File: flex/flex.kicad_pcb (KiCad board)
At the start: 2 copper layers, 104.8 x 90.6 mm, 73 parts, among them J1 Conn_01x04_Female, J2 Conn_01x05_Female, J3 Conn_01x03_Female, J4 Conn_01x06_Female, J5 Conn_01x03_Female, SW10 SW_Push, SW11 SW_Push, SW12 SW_Push, SW15 SW_Push, SW16 SW_Push, SW17 SW_Push, SW20 SW_Push, SW21 SW_Push, SW22 SW_Push, SW24 SW_Push, SW25 SW_Push, SW26 SW_Push, SW6 SW_Push, SW7 SW_Push, SW8 SW_Push

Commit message: licenses
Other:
- board text added: "Licensed under CC BY-NC-SA 4.0 Copyright Quentin Lebastard 2022"

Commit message: edge cuts
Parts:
- added C1: C, libs:D_0402, F.Cu at (43.2, 75.8)
- added D25: 1N4148, libs:D_SOD-523, F.Cu at (75.8, 122.1)
- added D26: 1N4148, libs:D_SOD-523, F.Cu at (75.8, 123.3)
- added D8: 1N4148, libs:D_SOD-523, F.Cu at (75.8, 124.6)
- added R1: R, libs:D_0402, F.Cu at (43.2, 74.5)
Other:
- board size 104.8 x 90.6 mm -> 104.1 x 90.6 mm

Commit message: PCB settigs
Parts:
- removed the C1 at (43.2, 75.8)
- removed the D25 at (75.8, 122.1)
- removed the D26 at (75.8, 123.3)
- removed the D8 at (75.8, 124.6)
- removed the R1 at (43.2, 74.5)
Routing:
- net Gnd: track 613.5 -> 0.00 mm, vias 22 -> 0
- net Vcc: track 601.7 -> 0.00 mm, vias 16 -> 0
- net row2: track 460.2 -> 0.00 mm, vias 5 -> 0
- net row4: track 347.7 -> 0.00 mm, vias 8 -> 0
- net row3: track 294.0 -> 0.00 mm, vias 3 -> 0
- net col2: track 288.4 -> 0.00 mm, vias 8 -> 0
- net col6: track 174.7 -> 0.00 mm, vias 7 -> 0
- net col5: track 158.5 -> 0.00 mm, vias 6 -> 0
- net col3: track 157.7 -> 0.00 mm, vias 7 -> 0
- net Net-(D41-Pad1): track 147.8 -> 0.00 mm, vias 3 -> 0
- net Net-(D25-Pad1): track 129.5 -> 0.00 mm, vias 2 -> 0
- net col4: track 128.3 -> 0.00 mm, vias 5 -> 0
- net Net-(D21-Pad3): track 122.1 -> 0.00 mm, vias 3 -> 0
- net Net-(D51-Pad1): track 103.0 -> 0.00 mm, vias 3 -> 0
- net Net-(D5-Pad3): track 54.8 -> 0.00 mm, vias 3 -> 0
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
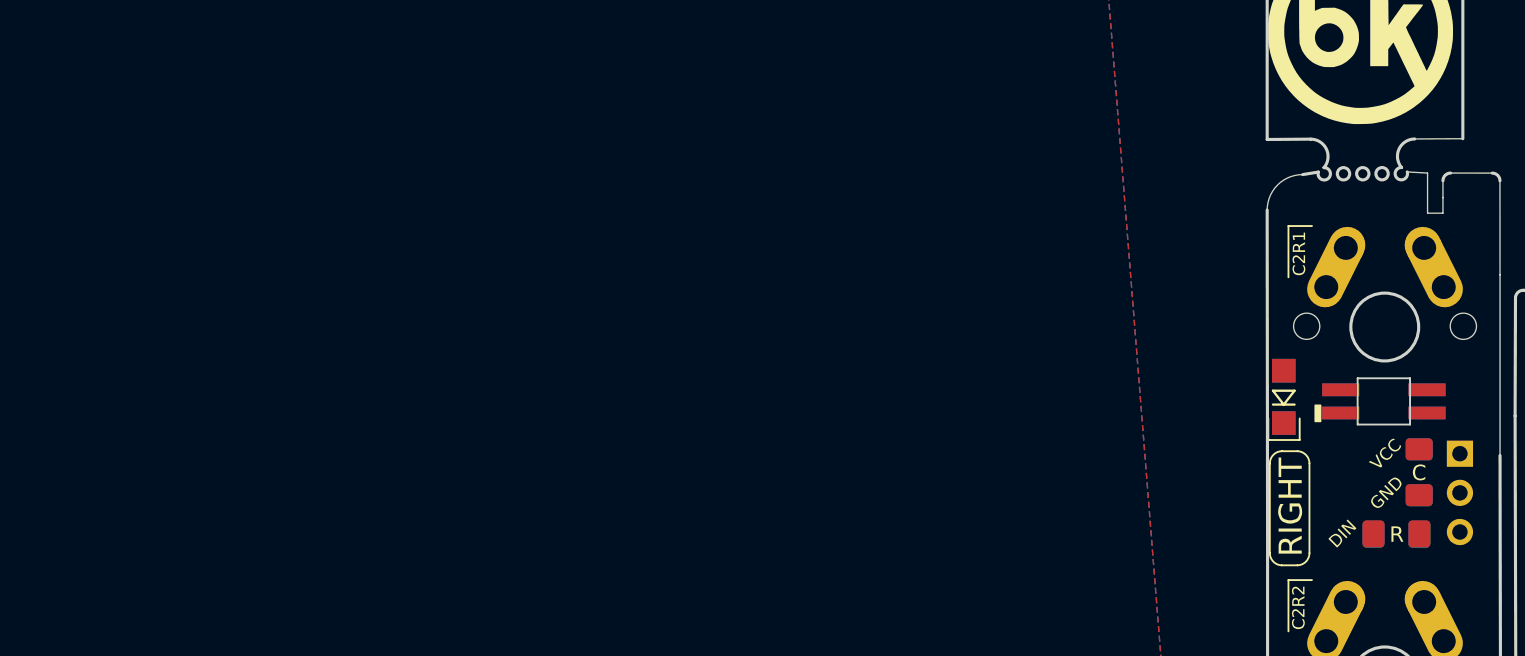
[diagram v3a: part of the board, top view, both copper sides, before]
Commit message: cleanup schem, reversible r and c
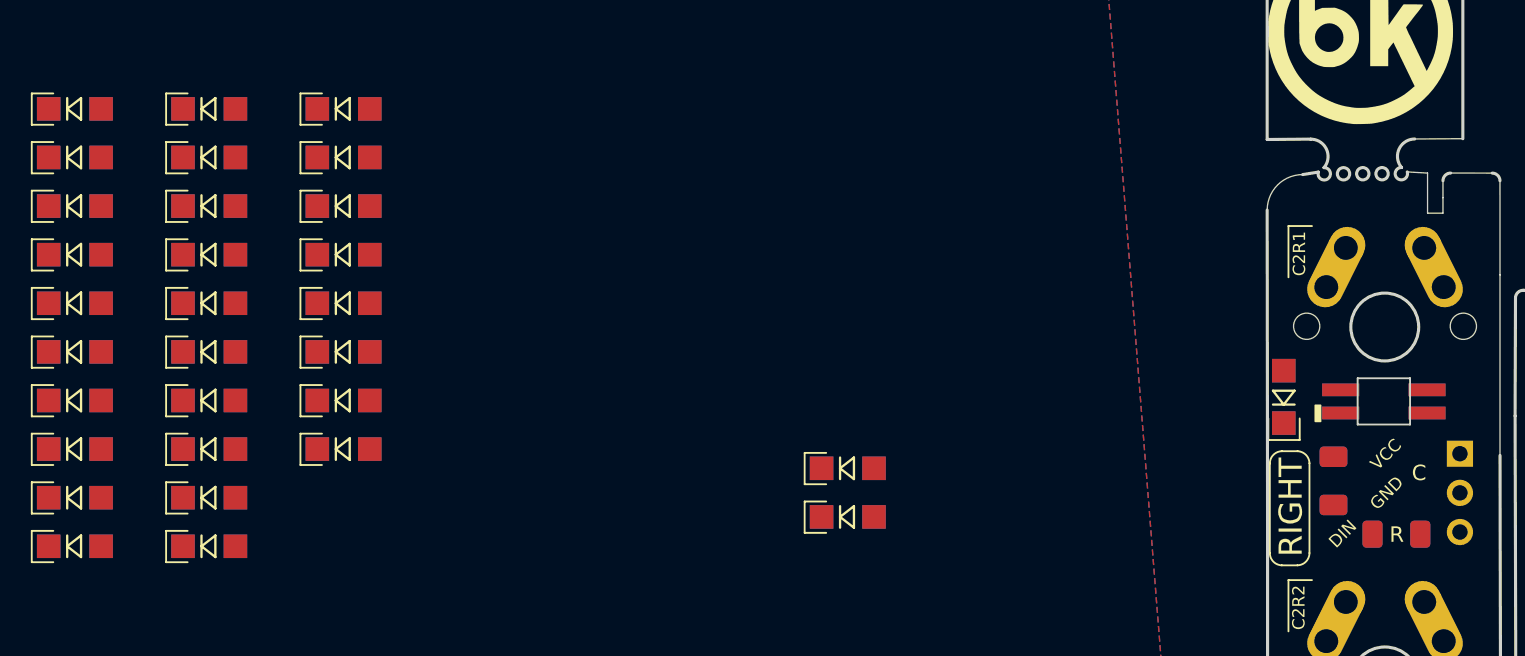
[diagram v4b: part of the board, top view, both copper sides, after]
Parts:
- removed C2: C, Capacitor_SMD:C_1206_3216Metric_Pad1.42x1.75mm_HandSolder
- removed R2: R, Resistor_SMD:R_1206_3216Metric_Pad1.42x1.75mm_HandSolder
- added D1: RIGHT_D, custom:Diode_TH_SOD123, F.Cu at (25.4, 87.4)
- added D10: RIGHT_D, custom:Diode_TH_SOD123, F.Cu at (-24.7, 70.4)
- added D18: LEFT_D, custom:Diode_TH_SOD123, F.Cu at (-24.7, 73.6)
- added D2: LEFT_D, custom:Diode_TH_SOD123, F.Cu at (25.4, 90.6)
- added D28: RIGHT_D, custom:Diode_TH_SOD123, F.Cu at (-24.7, 76.7)
- added D29: LEFT_D, custom:Diode_TH_SOD123, F.Cu at (-24.7, 79.9)
- added D3: RIGHT_D, custom:Diode_TH_SOD123, F.Cu at (-24.7, 64.1)
- added D30: RIGHT_D, custom:Diode_TH_SOD123, F.Cu at (-24.7, 83.0)
- added D4: LEFT_D, custom:Diode_TH_SOD123, F.Cu at (-24.7, 67.3)
- added D43: LEFT_D, custom:Diode_TH_SOD123, F.Cu at (-24.7, 86.2)
- added D44: RIGHT_D, custom:Diode_TH_SOD123, F.Cu at (-24.7, 89.4)
- added D45: LEFT_D, custom:Diode_TH_SOD123, F.Cu at (-24.7, 92.5)
- added D46: RIGHT_D, custom:Diode_TH_SOD123, F.Cu at (-16.0, 64.1)
- added D53: LEFT_D, custom:Diode_TH_SOD123, F.Cu at (-16.0, 67.3)
- added D54: RIGHT_D, custom:Diode_TH_SOD123, F.Cu at (-16.0, 70.4)
- added D61: LEFT_D, custom:Diode_TH_SOD123, F.Cu at (-16.0, 73.6)
- added D62: RIGHT_D, custom:Diode_TH_SOD123, F.Cu at (-16.0, 76.7)
- added D63: LEFT_D, custom:Diode_TH_SOD123, F.Cu at (-16.0, 79.9)
- added D64: RIGHT_D, custom:Diode_TH_SOD123, F.Cu at (-16.0, 83.0)
- added D65: LEFT_D, custom:Diode_TH_SOD123, F.Cu at (-16.0, 86.2)
- added D66: RIGHT_D, custom:Diode_TH_SOD123, F.Cu at (-16.0, 89.4)
- added D67: LEFT_D, custom:Diode_TH_SOD123, F.Cu at (-16.0, 92.5)
- added D68: RIGHT_D, custom:Diode_TH_SOD123, F.Cu at (-7.30, 64.1)
- added D69: LEFT_D, custom:Diode_TH_SOD123, F.Cu at (-7.30, 67.3)
- added D70: RIGHT_D, custom:Diode_TH_SOD123, F.Cu at (-7.30, 70.4)
- added D71: LEFT_D, custom:Diode_TH_SOD123, F.Cu at (-7.30, 73.6)
- added D72: RIGHT_D, custom:Diode_TH_SOD123, F.Cu at (-7.30, 76.7)
- added D73: LEFT_D, custom:Diode_TH_SOD123, F.Cu at (-7.30, 79.9)
- added D74: RIGHT_D, custom:Diode_TH_SOD123, F.Cu at (-7.30, 83.0)
- added D75: LEFT_D, custom:Diode_TH_SOD123, F.Cu at (-7.30, 86.2)
- C1: value C -> NA_C; footprint Capacitor_SMD:C_1206_3216Metric_Pad1.42x1.75mm_HandSolder -> custom:C_1206_3216Metric_Pad1.33x1.80mm_HandSolder_reversible; moved to B.Cu
- D11, D12, D13, D14, D15, D16, D17, D19, D20, D27, D31, D32, D35, D36, D9: value D -> NA_D
- R1: value R -> NA_R; footprint Resistor_SMD:R_1206_3216Metric_Pad1.42x1.75mm_HandSolder -> custom:R_1206_3216Metric_Pad1.30x1.75mm_HandSolder_reversible
- SW10, SW11, SW12, SW15, SW16, SW17, SW20, SW21, SW22, SW24, SW25, SW26, SW6, SW7, SW8: value SW_Push -> NA_SW_Push
- moved C1 5.58 mm to (61.9, 88.3)
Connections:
- D21 pad 2: Gnd -> Net-(D21-VSS)
- D21 pad 3: Net-(D21-Pad3) -> Net-(D21-DIN)
- D21 pad 4: Vcc -> Net-(D21-VDD)
- D22 pad 2: Gnd -> Net-(D22-VSS)
- D22 pad 3: Net-(D21-Pad3) -> Net-(D21-DIN)
- D22 pad 4: Vcc -> Net-(D22-VDD)
- D23 pad 2: Gnd -> Net-(D21-VSS)
- D23 pad 4: Vcc -> Net-(D21-VDD)
- D24 pad 2: Gnd -> Net-(D22-VSS)
- D24 pad 4: Vcc -> Net-(D22-VDD)
- D25 pad 2: Gnd -> Net-(D21-VSS)
- D25 pad 4: Vcc -> Net-(D21-VDD)
- D26 pad 2: Gnd -> Net-(D22-VSS)
- D26 pad 4: Vcc -> Net-(D22-VDD)
- D33 pad 1: Net-(D21-Pad3) -> Net-(D21-DIN)
- D33 pad 4: Vcc -> Net-(D33-VDD)
- D34 pad 1: Net-(D21-Pad3) -> unconnected-(D34-DOUT-Pad1)
- D37 pad 2: Gnd -> Net-(D21-VSS)
- D37 pad 4: Vcc -> Net-(D21-VDD)
- D38 pad 2: Gnd -> Net-(D22-VSS)
- D38 pad 4: Vcc -> Net-(D22-VDD)
- D39 pad 2: Gnd -> Net-(D21-VSS)
- D39 pad 4: Vcc -> Net-(D21-VDD)
- D40 pad 2: Gnd -> Net-(D22-VSS)
- D40 pad 4: Vcc -> Net-(D22-VDD)
- D41 pad 1: Net-(D41-Pad1) -> Net-(D41-DOUT)
- D41 pad 2: Gnd -> Net-(D21-VSS)
- D41 pad 4: Vcc -> Net-(D21-VDD)
- D42 pad 1: Net-(D41-Pad1) -> Net-(D42-DOUT)
- D42 pad 2: Gnd -> Net-(D22-VSS)
- D42 pad 4: Vcc -> Net-(D22-VDD)
- D47 pad 2: Gnd -> Net-(D21-VSS)
- D47 pad 3: Net-(D41-Pad1) -> Net-(D41-DOUT)
- D47 pad 4: Vcc -> Net-(D47-VDD)
- D48 pad 2: Gnd -> Net-(D48-VSS)
- D48 pad 3: Net-(D41-Pad1) -> Net-(D42-DOUT)
- D48 pad 4: Vcc -> Net-(D48-VDD)
- D49 pad 2: Gnd -> Net-(D21-VSS)
- D49 pad 4: Vcc -> Net-(D47-VDD)
- D5 pad 3: Net-(D5-Pad3) -> Net-(D5-DIN)
- D5 pad 4: Vcc -> Net-(D33-VDD)
- D50 pad 2: Gnd -> Net-(D48-VSS)
- D50 pad 4: Vcc -> Net-(D48-VDD)
- D51 pad 2: Gnd -> Net-(D21-VSS)
- D51 pad 4: Vcc -> Net-(D47-VDD)
- D52 pad 2: Gnd -> Net-(D48-VSS)
- D52 pad 4: Vcc -> Net-(D48-VDD)
- D55 pad 2: Gnd -> Net-(D55-VSS)
- D55 pad 4: Vcc -> Net-(D47-VDD)
- D56 pad 2: Gnd -> Net-(D48-VSS)
- D56 pad 4: Vcc -> Net-(D48-VDD)
- D57 pad 2: Gnd -> Net-(D55-VSS)
- D57 pad 4: Vcc -> Net-(D47-VDD)
- D58 pad 2: Gnd -> Net-(D48-VSS)
- D58 pad 4: Vcc -> Net-(D48-VDD)
- D59 pad 2: Gnd -> Net-(D55-VSS)
- D59 pad 4: Vcc -> Net-(D47-VDD)
- D6 pad 3: Net-(D5-Pad3) -> Net-(D5-DIN)
- D60 pad 2: Gnd -> Net-(D48-VSS)
- D60 pad 4: Vcc -> Net-(D48-VDD)
- D7 pad 4: Vcc -> Net-(D33-VDD)
- J2 pad 4: col1 -> unconnected-(J2-Pin_4-Pad4)
- R1 pad 2: Net-(D5-Pad3) -> unconnected-(R1-Pad2)

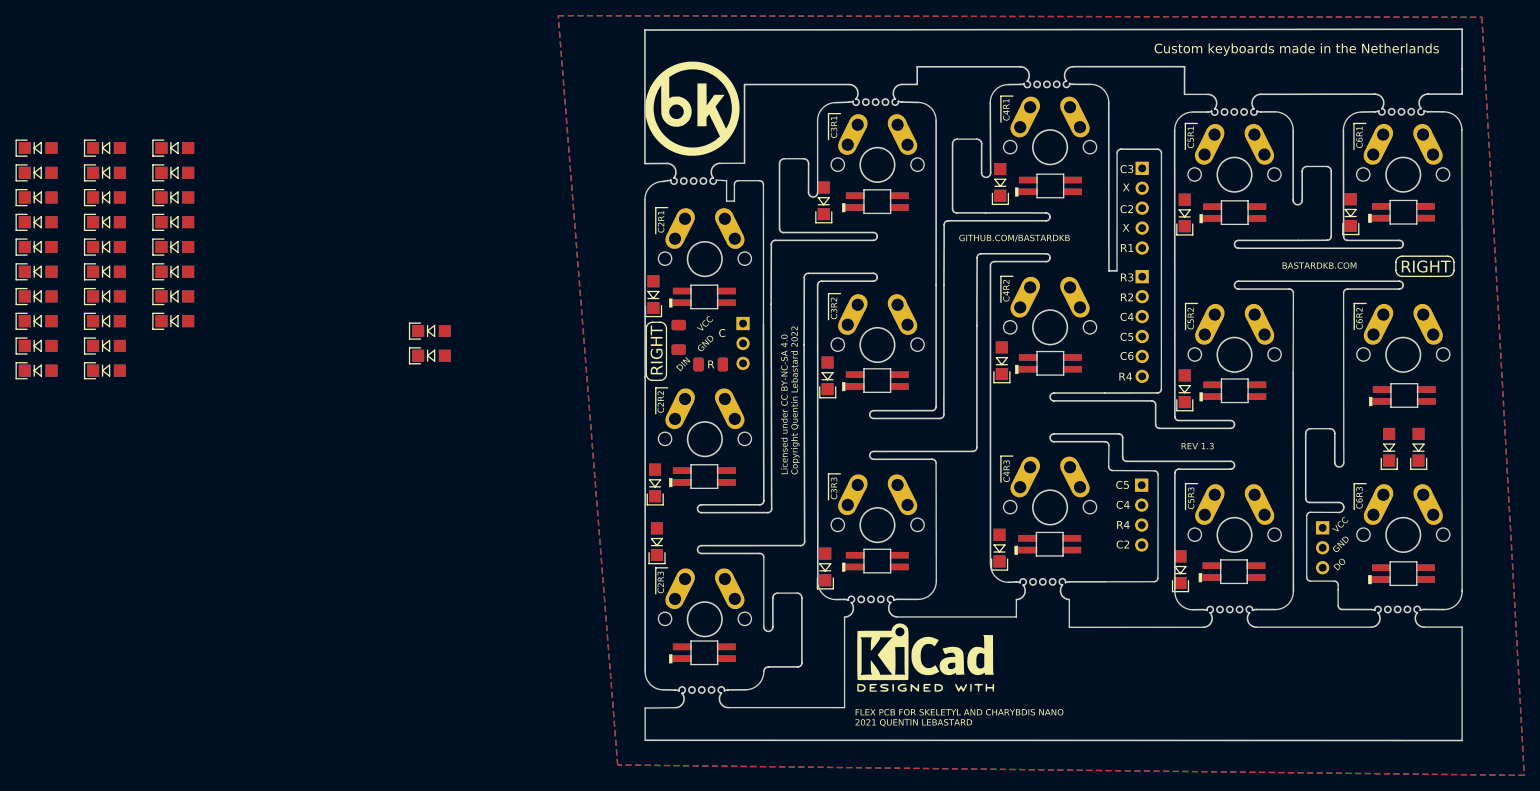
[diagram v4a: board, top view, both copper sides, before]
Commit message: place smd components
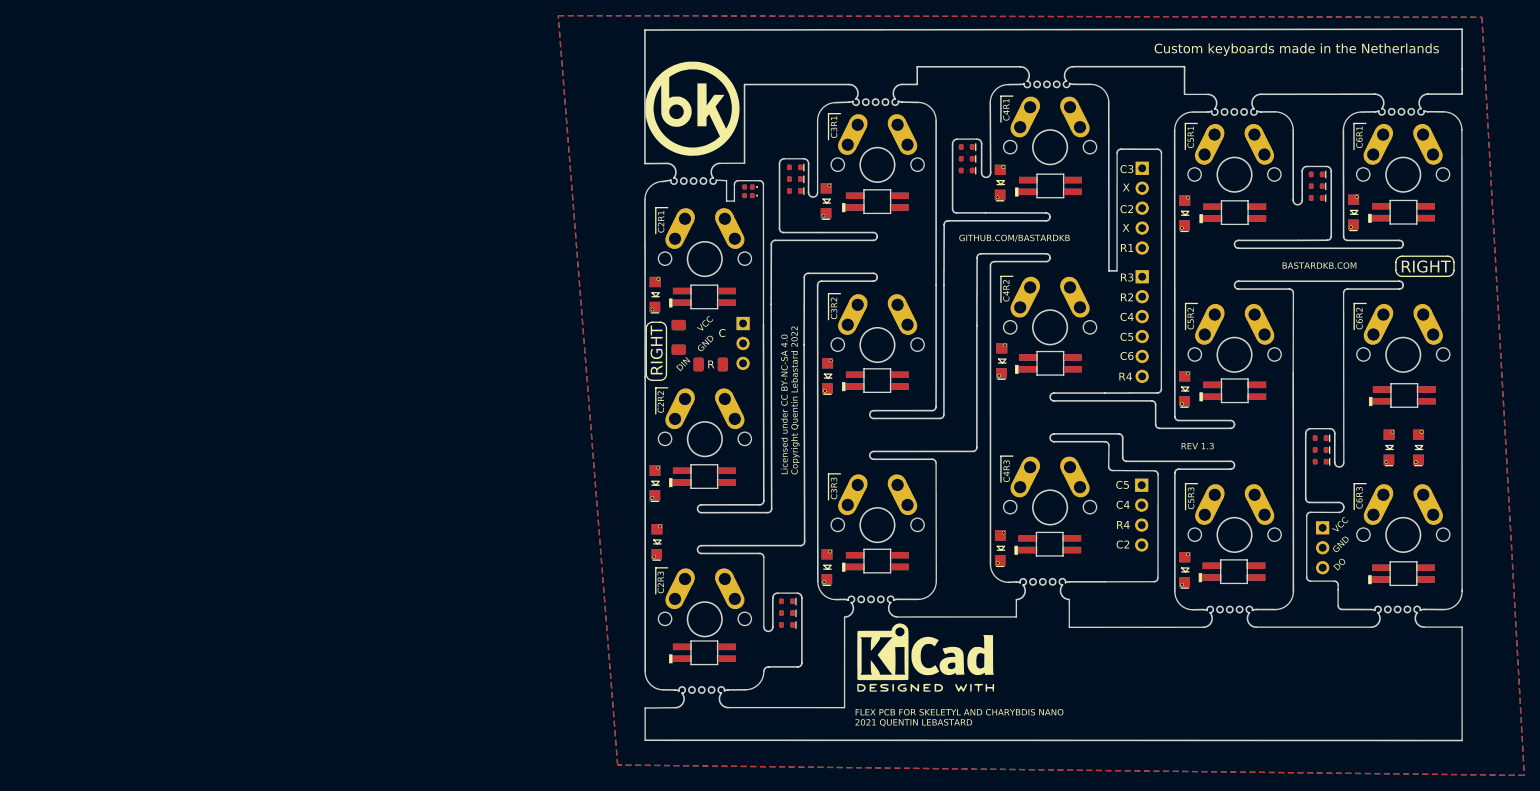
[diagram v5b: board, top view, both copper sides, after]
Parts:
- added C2: RIGHT_C, custom:R_0402, F.Cu at (70.8, 69.1)
- added C3: LEFT_C, custom:R_0402, B.Cu at (70.8, 69.1)
- added R2: RIGHT_R, custom:R_0402, F.Cu at (70.8, 70.2)
- added R3: LEFT_R, custom:R_0402, B.Cu at (70.8, 70.2)
- D1, D10, D28, D3, D30, D44, D46, D54, D62, D64, D66, D68, D70, D72, D74: footprint custom:Diode_TH_SOD123 -> custom:D_SOD-523
- D18, D2, D29, D4, D43, D45, D53, D61, D63, D65, D67, D69, D71, D73, D75: footprint custom:Diode_TH_SOD123 -> custom:D_SOD-523; moved to B.Cu
- moved D3 172.8 mm to (143.7, 102.6), turned to 180 degrees
- moved D4 172.1 mm to (143.7, 102.6), turned to 180 degrees
- moved D10 171.8 mm to (143.7, 104.1), turned to 180 degrees
- moved D18 171.2 mm to (143.7, 104.1), turned to 180 degrees
- moved D45 169.4 mm to (143.2, 70.5), turned to 180 degrees
- moved D44 169.0 mm to (143.2, 70.5), turned to 180 degrees
- moved D43 168.8 mm to (143.2, 69.0), turned to 180 degrees
- moved D30 168.5 mm to (143.2, 69.0), turned to 180 degrees
- moved D29 168.4 mm to (143.2, 67.5), turned to 180 degrees
- moved D28 168.2 mm to (143.2, 67.5), turned to 180 degrees
- moved D1 119.1 mm to (143.7, 101.1), turned to 180 degrees
- moved D2 118.8 mm to (143.7, 101.1), turned to 180 degrees
- moved D63 115.3 mm to (98.6, 67.0), turned to 180 degrees
- moved D62 115.0 mm to (98.6, 67.0), turned to 180 degrees
- moved D61 114.9 mm to (98.6, 65.5), turned to 180 degrees
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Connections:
- R1 pad 2: unconnected-(R1-Pad2) -> Net-(R1-Pad2)
